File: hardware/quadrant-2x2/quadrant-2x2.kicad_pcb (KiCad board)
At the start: 4 copper layers, 120 x 108 mm, 129 parts, among them J1 FPC 16, P1 NPTH, Q1 AO3401A, Q111 AO3400A, Q112 AO3401A, Q121 AO3400A, Q122 AO3401A, Q131 AO3400A, Q132 AO3401A, Q141 AO3400A, Q142 AO3401A, Q2 AO3400A, U1 74HC4514, U2 74HC154, U3 ADG1607, U5 AD8421, U6 74LVC1G04, U7 OPA2810, U8 OPA2810

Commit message: Quadrant 2 x 2 reroutée : 7 éléments non connectés au DRC de KiCad, contre 117
La bande de frontal est reroutée sur la comptabilité de connexité
partagée, avec la géométrie qui rendait le routage impossible corrigée
à la racine (note 04) : bus réespacés pour qu'un via puisse les
atteindre et prolongés jusqu'aux amplificateurs, plan de masse sur la
couche arrière à la place du bus de masse, prises des cellules
dessinées dans le générateur (masse, 5VA, référence, bus d'excitation,
12 V, entrées d'aiguilleur, grille d'excitation), chaîne LED sortie de
la bande par deux voies, placement du frontal par affinité.

Le compte du build et celui de KiCad disent désormais la même chose.
Restent sept liaisons, listées une par une dans le README de la carte
avec leurs coordonnées : PULSE_EN (trois pastilles), M2_A, DAMP4_N,
INA_INP et un via de masse isolé dans une crique du plan.

Deux faces tracées par KiCad ajoutées au README, notes 04, 07, 08, 19
et 20 mises à jour, tests de couloir de via et de géométrie de la
bande ajoutés.
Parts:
- moved C20 81.7 mm to (2.28, 100.5), turned to 0 degrees
- moved R24 80.2 mm to (2.28, 102.2), turned to 0 degrees
- moved R21 77.2 mm to (5.49, 100.5), turned to 0 degrees
- moved R22 77.1 mm to (8.70, 100.5), turned to 0 degrees
- moved C21 77.0 mm to (11.9, 100.5), turned to 0 degrees
- moved R23 77.0 mm to (15.1, 100.5), turned to 0 degrees
- moved R20 75.7 mm to (17.4, 95.9)
- moved C19 75.2 mm to (9.48, 95.2)
- moved R19 72.6 mm to (17.4, 92.7)
- moved R18 69.5 mm to (17.4, 89.5)
- moved R17 65.9 mm to (15.1, 85.9), turned to 0 degrees
- moved R16 65.8 mm to (11.9, 85.9), turned to 0 degrees
- moved R15 65.7 mm to (8.70, 85.9), turned to 0 degrees
- moved C18 65.6 mm to (5.49, 85.9), turned to 0 degrees
- moved C17 65.6 mm to (2.28, 85.9), turned to 0 degrees
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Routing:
- net 5VA: track 116.5 -> 242.9 mm, vias 9 -> 23
- net GND: track 740.0 -> 630.6 mm, vias 29 -> 71
- net 3V3: track 54.4 -> 148.5 mm, vias 8 -> 9
- net MUX_A1: track 6.94 -> 96.3 mm, vias 4 -> 5
- net MUX_A2: track 8.34 -> 95.0 mm
- net M2_B: track 0.71 -> 82.4 mm, vias 0 -> 11
- net MUX_A0: track 6.84 -> 88.4 mm, vias 3 -> 7
- net OUT_STAGE: track 93.9 -> 13.6 mm
- net M4_A: track 1.51 -> 81.8 mm, vias 1 -> 6
- net LP_OUT: track 94.5 -> 16.6 mm, vias 6 -> 4
- net HP_IN: track 85.1 -> 9.60 mm, vias 6 -> 2
- net MUX_EN_L: track 3.26 -> 77.9 mm, vias 2 -> 7
- net PULSE_EN: track 73.1 -> 1.75 mm, vias 3 -> 1
- net M1_B: track 1.51 -> 71.5 mm, vias 1 -> 7
- net M1_A: track 0.71 -> 68.9 mm, vias 0 -> 4
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- added copper zone on B.Cu, net GND
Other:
- board text added: "DAMIER LC / QUADRANT 2x2 / p50"
- board text removed: "DAMIER LC / QUADRANT 4x4 / p50"

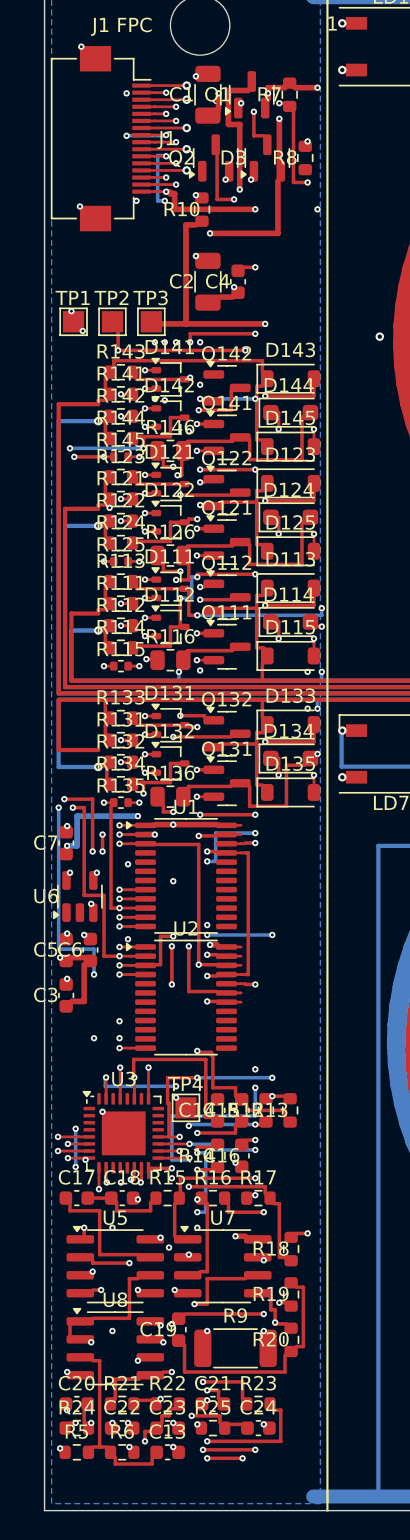
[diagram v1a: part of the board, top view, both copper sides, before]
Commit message: Quadrant 2 x 2 : les sept dernières liaisons tracées à la main, DRC de KiCad à zéro
Le routeur du frontal ne pouvait pas les trouver, et chacune avait sa
raison : un chas de 0,475 mm dans le champ d'échappées du connecteur là
où une piste de 0,25 avec ses deux gardes en demande 0,55, deux nappes
longues comme la bande que nul coût local ne choisit, quatre pastilles
de la colonne d'amplification que les deux rails analogiques enjambent
sans laisser la place d'un via, et une crique du plan de masse dont la
descente n'atteignait que du cuivre que le remplisseur retire.

Les sept sont dans tools/quadgen/hand.py, dessinées avant le routage
comme les prises des cellules : le build les redessine et les vérifie à
chaque fois, et le routeur route tout le reste autour d'elles. Trois
n'étaient apparues qu'après le tracé des premières, chaque nappe posée
déplaçant les choix du routeur ; neuf routages complets ont été
nécessaires, encadrés par une vérification de géométrie de cinq
secondes avant routage.

DRC KiCad 7 du quadrant 2 x 2 : 395 signalements, zéro erreur et zéro
élément non connecté, contre 117 le matin même et sept après le
reroutage. Le compte du build dit la même chose.

- quadgen/hand.py : les liaisons, placées depuis les pastilles réelles ;
  quadgen/variant.py : is_reduced, ces tracés appartenant à la carte en
  fabrication, le 4 x 4 agençant sa bande autrement
- tests : test_reduced_strip_geometry_is_legal_before_routing applique
  le contrôle d'isolement exact au cuivre posé avant routage
- note 04 : pourquoi chacune est hors de portée du routeur et ce que
  chaque nappe déplace ; notes 07, 14, 20 et README de la carte à jour
- hardware/quadrant-2x2 et les deux faces tracées régénérés
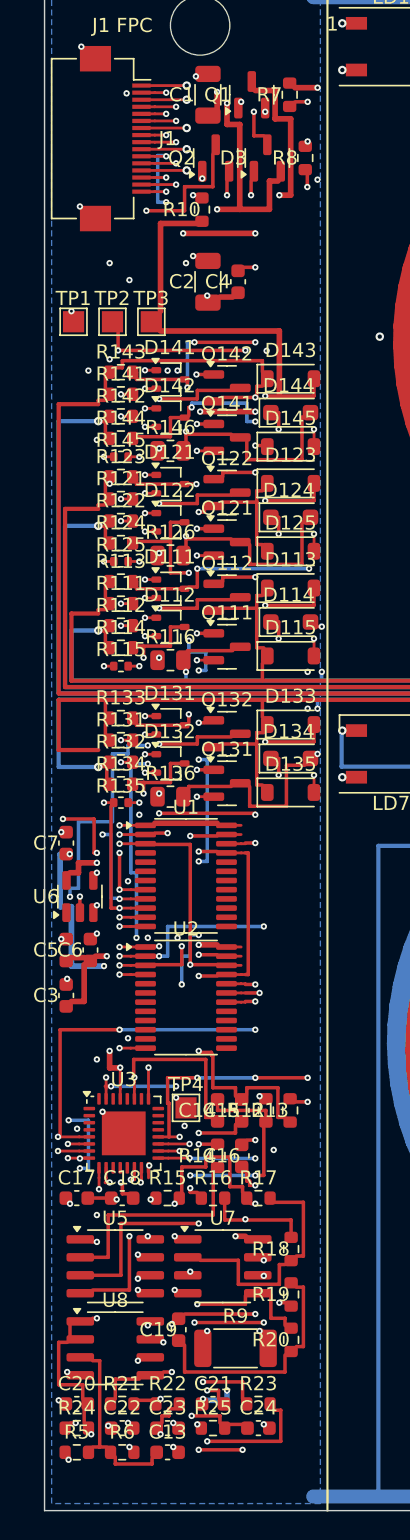
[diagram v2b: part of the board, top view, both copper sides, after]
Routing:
- net PULSE_EN: track 1.75 -> 74.2 mm, vias 1 -> 4
- net DAMP4_N: track 1.84 -> 55.3 mm, vias 1 -> 2
- net M2_A: track 5.70 -> 56.3 mm, vias 1 -> 2
- net M1_B: track 71.5 -> 50.6 mm, vias 7 -> 6
- net GND: track 630.6 -> 650.8 mm
- net M4_B: track 68.3 -> 83.1 mm
- net Q1_G: track 19.8 -> 33.5 mm, vias 4 -> 3
- net 5VA: track 242.9 -> 255.2 mm, vias 23 -> 25
- net M2_B: track 82.4 -> 70.4 mm, vias 11 -> 8
- net DRIVE4: track 50.5 -> 61.1 mm, vias 6 -> 8
- net VIN: track 79.9 -> 90.4 mm, vias 10 -> 12
- net M3_A: track 48.1 -> 41.0 mm, vias 5 -> 7
- net LP_IN: track 29.6 -> 23.8 mm, vias 4 -> 2
- net M4_A: track 81.8 -> 86.6 mm, vias 6 -> 7
- net DRIVE_BUS: track 108.2 -> 112.8 mm, vias 7 -> 6
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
